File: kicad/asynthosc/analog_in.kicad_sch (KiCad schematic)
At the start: 14 parts, among them J6 AudioJack3, U8 MCP6004, U9 MCP6004

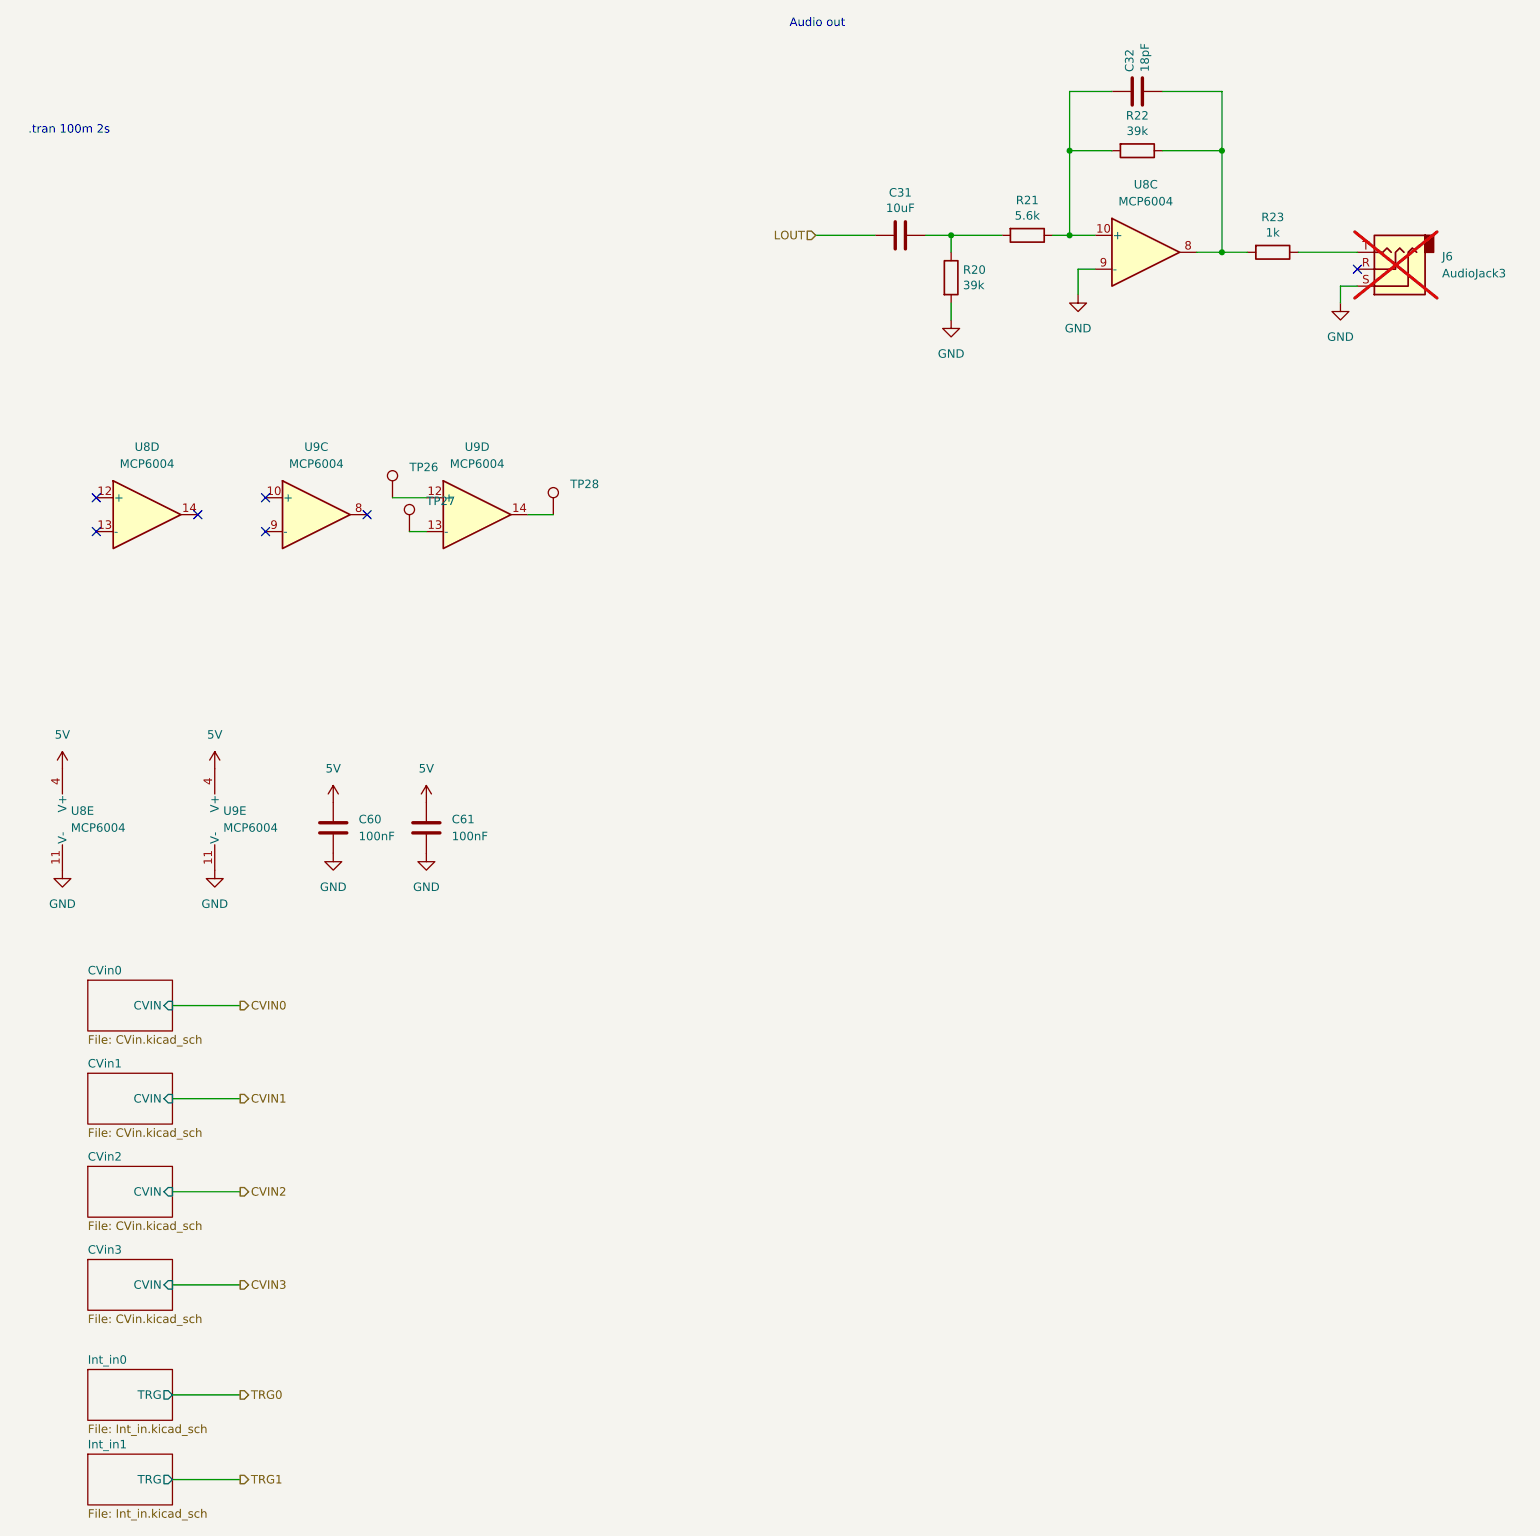
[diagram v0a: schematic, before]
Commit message: bom: fab: switch component due to fab shortage
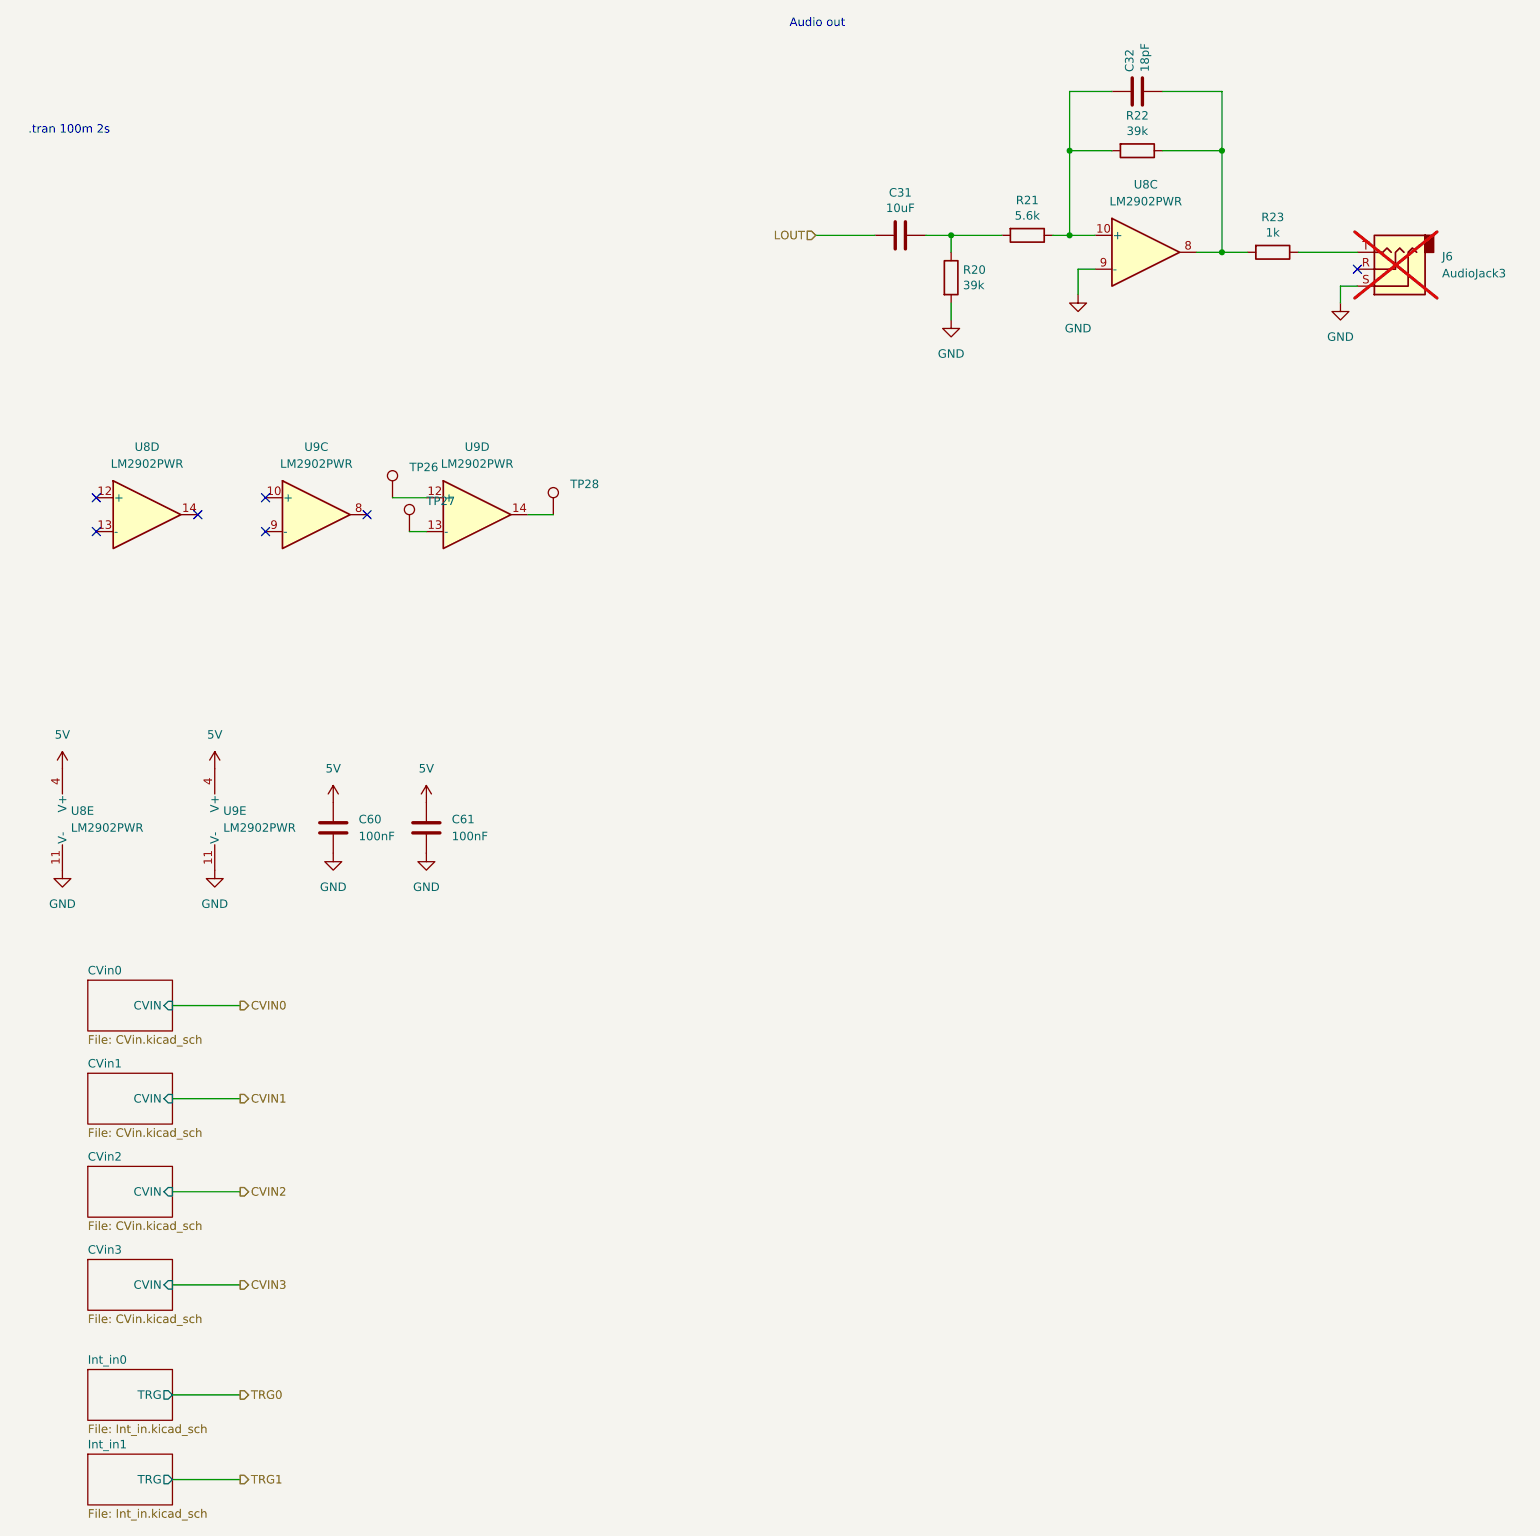
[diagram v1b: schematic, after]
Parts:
- U8, U9: value MCP6004 -> LM2902PWR; LCSC C627416 -> C46864; Manufacturer Microchip -> TI; RefNum MCP6004T-E/ST -> LM2902PWR
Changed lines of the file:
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@@
 			)
 		)
-		(property "Value" "MCP6004"
+		(property "Value" "LM2902PWR"
 			(at 30.48 151.1299 0)
 			(effects
@@
 			)
 		)
-		(property "LCSC" "C627416"
+		(property "LCSC" "C46864"
 			(at 31.75 149.86 0)
 			(effects
@@
 			)
 		)
-		(property "Manufacturer" "Microchip"
+		(property "Manufacturer" "TI"
 			(at 31.75 149.86 0)
 			(effects
@@
 			)
 		)
-		(property "RefNum" " MCP6004T-E/ST"
+		(property "RefNum" " LM2902PWR"
 			(at 31.75 149.86 0)
 			(effects
@@
 			)
 		)
-		(property "Value" "MCP6004"
+		(property "Value" "LM2902PWR"
 			(at 67.31 96.52 0)
 			(effects
@@
 			)
 		)
-		(property "LCSC" "C627416"
+		(property "LCSC" "C46864"
 			(at 67.31 104.14 0)
 			(effects
@@
 			)
 		)
-		(property "Manufacturer" "Microchip"
+		(property "Manufacturer" "TI"
 			(at 67.31 104.14 0)
 			(effects
@@
 			)
 		)
-		(property "RefNum" " MCP6004T-E/ST"
+		(property "RefNum" " LM2902PWR"
 			(at 67.31 104.14 0)
 			(effects
@@
 			)
 		)
-		(property "Value" "MCP6004"
+		(property "Value" "LM2902PWR"
 			(at 41.91 96.52 0)
 			(effects
@@
 			)
 		)
-		(property "LCSC" "C627416"
+		(property "LCSC" "C46864"
 			(at 41.91 104.14 0)
 			(effects
@@
 			)
 		)
-		(property "Manufacturer" "Microchip"
+		(property "Manufacturer" "TI"
 			(at 41.91 104.14 0)
 			(effects
@@
 			)
 		)
-		(property "RefNum" " MCP6004T-E/ST"
+		(property "RefNum" " LM2902PWR"
 			(at 41.91 104.14 0)
 			(effects
@@
 			)
 		)
-		(property "Value" "MCP6004"
+		(property "Value" "LM2902PWR"
 			(at 53.34 151.1299 0)
 			(effects
@@
 			)
 		)
-		(property "LCSC" "C627416"
+		(property "LCSC" "C46864"
 			(at 54.61 149.86 0)
 			(effects
@@
 			)
 		)
-		(property "Manufacturer" "Microchip"
+		(property "Manufacturer" "TI"
 			(at 54.61 149.86 0)
 			(effects
@@
 			)
 		)
-		(property "RefNum" " MCP6004T-E/ST"
+		(property "RefNum" " LM2902PWR"
 			(at 54.61 149.86 0)
 			(effects
@@
 			)
 		)
-		(property "Value" "MCP6004"
+		(property "Value" "LM2902PWR"
 			(at 91.44 96.52 0)
 			(effects
@@
 			)
 		)
-		(property "LCSC" "C627416"
+		(property "LCSC" "C46864"
 			(at 91.44 104.14 0)
 			(effects
@@
 			)
 		)
-		(property "Manufacturer" "Microchip"
+		(property "Manufacturer" "TI"
 			(at 91.44 104.14 0)
 			(effects
@@
 			)
 		)
-		(property "RefNum" " MCP6004T-E/ST"
+		(property "RefNum" " LM2902PWR"
 			(at 91.44 104.14 0)
 			(effects
@@
 			)
 		)
-		(property "Value" "MCP6004"
+		(property "Value" "LM2902PWR"
 			(at 191.77 57.15 0)
 			(effects
@@
 			)
 		)
-		(property "LCSC" "C627416"
+		(property "LCSC" "C46864"
 			(at 191.77 64.77 0)
 			(effects
@@
 			)
 		)
-		(property "Manufacturer" "Microchip"
+		(property "Manufacturer" "TI"
 			(at 191.77 64.77 0)
 			(effects
@@
 			)
 		)
-		(property "RefNum" " MCP6004T-E/ST"
+		(property "RefNum" " LM2902PWR"
 			(at 191.77 64.77 0)
 			(effects
